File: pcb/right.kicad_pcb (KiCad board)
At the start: 2 copper layers, 135 x 95.7 mm, 50 parts, among them SW1 SW_PUSH, SW10 SW_PUSH, SW11 SW_PUSH, SW12 SW_PUSH, SW13 SW_PUSH, SW14 SW_PUSH, SW15 SW_PUSH, SW16 SW_PUSH, SW17 SW_PUSH, SW18 SW_PUSH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

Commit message: update cases, extra hole on right side
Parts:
- added H8: MountingHole, kbd:M2_HOLE_v2, F.Cu at (91.0, 61.0)
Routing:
- net col3: track 137.9 -> 136.3 mm
- net ENCB: track 63.0 -> 64.1 mm
- net col4: track 113.5 -> 113.0 mm

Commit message: improve rotary encoder footprint
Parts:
- RE1: footprint pica:RotaryEncoder_EC11-no-legs -> pica:RotaryEncoder_EC11
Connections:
- RE1 pad S1: unconnected-(RE1-PadS1) -> (no net)
- RE1 pad S2: unconnected-(RE1-PadS2) -> (no net)
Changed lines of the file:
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@@
   (net 32 "row6")
   (net 33 "row7")
-  (net 34 "unconnected-(RE1-PadS2)")
-  (net 35 "unconnected-(RE1-PadS1)")
   (footprint "pica:CherryMX_Hotswap" (layer "F.Cu")
     (at 153 99)
@@
     )
   )
-  (footprint "pica:RotaryEncoder_EC11-no-legs" (layer "F.Cu")
+  (footprint "pica:RotaryEncoder_EC11" (layer "F.Cu")
     (at 95.5 74 -90)
     (descr "Alps rotary encoder, EC12E... with switch, vertical shaft, http://www.alps.com/prod/info/E/HTML/Encoder/Incremental/EC11/EC11E15204A3.html")
@@
     (property "Sheetname" "")
     (attr through_hole)
-    (fp_text reference "RE1" (at -4.7 -7.2 90) (layer "F.Fab")
+    (fp_text reference "RE1" (at -4.7 -7.2 -90) (layer "F.Fab")
       (effects (font (size 1 1) (thickness 0.15)))
     )
-    (fp_text value "RotaryEncoder_Switch" (at 0 7.9 90) (layer "F.Fab")
-      (effects (font (size 1 1) (thickness 0.15)))
-    )
-    (fp_text user "${REFERENCE}" (at 3.6 3.8 90) (layer "F.Fab")
+    (fp_text value "RotaryEncoder_Switch" (at 0 7.9 -90) (layer "F.Fab")
       (effects (font (size 1 1) (thickness 0.15)))
     )
+    (fp_line (start -0.5 0) (end 0.5 0) (layer "F.SilkS") (width 0.12))
+    (fp_line (start 6.1 5.9) (end 2 5.9) (layer "F.SilkS") (width 0.12))
     (fp_line (start -2 5.9) (end -6.1 5.9) (layer "F.SilkS") (width 0.12))
+    (fp_line (start 6.1 3.5) (end 6.1 5.9) (layer "F.SilkS") (width 0.12))
     (fp_line (start 6.1 -5.9) (end 6.1 -3.5) (layer "F.SilkS") (width 0.12))
-    (fp_line (start 6.1 5.9) (end 2 5.9) (layer "F.SilkS") (width 0.12))
+    (fp_line (start -6.1 -5.9) (end -6.1 5.9) (layer "F.SilkS") (width 0.12))
     (fp_line (start -2 -5.9) (end -6.1 -5.9) (layer "F.SilkS") (width 0.12))
     (fp_line (start 0 -0.5) (end 0 0.5) (layer "F.SilkS") (width 0.12))
-    (fp_line (start -6.1 -5.9) (end -6.1 5.9) (layer "F.SilkS") (width 0.12))
     (fp_line (start 6.1 -1.3) (end 6.1 1.3) (layer "F.SilkS") (width 0.12))
-    (fp_line (start -0.5 0) (end 0.5 0) (layer "F.SilkS") (width 0.12))
     (fp_line (start 2 -5.9) (end 6.1 -5.9) (layer "F.SilkS") (width 0.12))
-    (fp_line (start 6.1 3.5) (end 6.1 5.9) (layer "F.SilkS") (width 0.12))
     (fp_circle (center 0 0) (end 3 0) (layer "F.SilkS") (width 0.12) (fill none))
-    (fp_line (start 8.5 7.1) (end 8.5 -7.1) (layer "F.CrtYd") (width 0.05))
     (fp_line (start -9 -7.1) (end 8.5 -7.1) (layer "F.CrtYd") (width 0.05))
     (fp_line (start -9 -7.1) (end -9 7.1) (layer "F.CrtYd") (width 0.05))
     (fp_line (start 8.5 7.1) (end -9 7.1) (layer "F.CrtYd") (width 0.05))
-    (fp_line (start 6 5.8) (end -6 5.8) (layer "F.Fab") (width 0.12))
-    (fp_line (start 6 -5.8) (end 6 5.8) (layer "F.Fab") (width 0.12))
-    (fp_line (start -6 5.8) (end -6 -4.7) (layer "F.Fab") (width 0.12))
+    (fp_line (start 8.5 7.1) (end 8.5 -7.1) (layer "F.CrtYd") (width 0.05))
     (fp_line (start -6 -4.7) (end -5 -5.8) (layer "F.Fab") (width 0.12))
+    (fp_line (start 0 -3) (end 0 3) (layer "F.Fab") (width 0.12))
+    (fp_line (start -6 5.8) (end -6 -4.7) (layer "F.Fab") (width 0.12))
+    (fp_line (start 6 -5.8) (end 6 5.8) (layer "F.Fab") (width 0.12))
+    (fp_line (start -3 0) (end 3 0) (layer "F.Fab") (width 0.12))
     (fp_line (start -5 -5.8) (end 6 -5.8) (layer "F.Fab") (width 0.12))
+    (fp_line (start 6 5.8) (end -6 5.8) (layer "F.Fab") (width 0.12))
+    (fp_circle (center 0 0) (end 3 0) (layer "F.Fab") (width 0.12) (fill none))
+    (pad "" np_thru_hole oval (at 0 5.6 270) (size 3.2 2) (drill oval 2.8 1.5) (layers F&B.Cu "B.Mask"))
+    (pad "" np_thru_hole oval (at 0 -5.6 270) (size 3.2 2) (drill oval 2.8 1.5) (layers F&B.Cu "B.Mask"))
     (pad "A" thru_hole circle (at -7.5 -2.5 270) (size 2 2) (drill 1) (layers *.Cu "B.SilkS" "B.Mask")
       (net 24 "ENCA") (pinfunction "A") (pintype "passive"))
@@
       (net 2 "GND") (pinfunction "C") (pintype "passive"))
     (pad "S1" thru_hole circle (at 7 2.5 270) (size 2 2) (drill 1) (layers *.Cu "B.Mask")
-      (net 35 "unconnected-(RE1-PadS1)") (pinfunction "S1") (pintype "passive+no_connect"))
+      (pinfunction "S1") (pintype "passive+no_connect"))
     (pad "S2" thru_hole circle (at 7 -2.5 270) (size 2 2) (drill 1) (layers *.Cu "B.Mask")
-      (net 34 "unconnected-(RE1-PadS2)") (pinfunction "S2") (pintype "passive+no_connect"))
+      (pinfunction "S2") (pintype "passive+no_connect"))
     (model "../footprints/Rotary Encoder.step"
       (offset (xyz -6 6 0))

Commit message: v2
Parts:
- removed H8: MountingHole, kbd:M2_HOLE_v2
- added BATTCONN1: Conn_01x02_Female, pica:JST_PH_S2B-PH-K_1x02_P2.00mm, F.Cu at (88.0, 81.3)
- added BATTCONN2: Conn_01x02_Female, pica:JST_PH_S2B-PH-K_1x02_P2.00mm, F.Cu at (145.0, 102.8)
- added BATTSW1: SW_SPDT, Button_Switch_SMD:SW_SPDT_PCM12, F.Cu at (84.0, 76.8)
- added JP1: SolderJumper_2_Open, Jumper:SolderJumper-2_P1.3mm_Open_TrianglePad1.0x1.5mm, B.Cu at (97.7, 81.6)
- added JP2: SolderJumper_2_Open, Jumper:SolderJumper-2_P1.3mm_Open_TrianglePad1.0x1.5mm, F.Cu at (97.7, 81.6)
- added RE2: RotaryEncoder_Switch, pica:RotaryEncoder_EC11, F.Cu at (160.2, 113.6)
- added U1: xiao-ble, pica:xiao-ble-tht, F.Cu at (92.0, 61.9)
- G***: moved to B.Cu
- H1, H2, H3, H4, H5: footprint kbd:M2_HOLE_v2 -> pica:spacer_m2_3.4
- H6, H7: footprint kbd:M2_Hole_TH -> kbd:thread_m2
- SW1, SW10, SW11, SW12, SW13, SW14, SW15, SW16, SW17, SW18, SW19, SW2, SW3, SW4, SW5, SW6, SW7, SW8, SW9: footprint pica:CherryMX_Hotswap -> pica:CherryMX_Hotswap_ChocV2
- SW20: footprint pica:CherryMX_Hotswap_1.5 -> pica:CherryMX_Hotswap_ChocV2_1.5
- USB1: footprint typec:HRO-TYPE-C-31-M-12-HandSoldering -> pica:HRO-TYPE-C-31-M-12-data
- moved H6 32.1 mm to (97.5, 74.8)
- moved H7 31.9 mm to (88.7, 74.8)
- moved RE1 20.5 mm to (91.5, 94.1), turned to 180 degrees
- moved D18 10.0 mm to (140.4, 104.8)
- moved D12 9.81 mm to (168.4, 101.8)
- moved D13 9.81 mm to (149.4, 97.8)
- moved D7 9.81 mm to (168.4, 82.8)
- moved D8 9.81 mm to (149.4, 78.8)
- moved H4 9.81 mm to (157.9, 99.8)
- moved SW12 9.81 mm to (168.4, 93.8)
- moved SW13 9.81 mm to (149.4, 89.8)
- moved SW18 9.81 mm to (140.4, 113.3)
- moved SW7 9.81 mm to (168.4, 74.8)
- moved SW8 9.81 mm to (149.4, 70.8)
- moved D10 9.81 mm to (111.5, 85.3)
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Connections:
- D1 pad 1: row7 -> row0_r
- D10 pad 1: row6 -> row1_r
- D11 pad 1: row5 -> row2_r
- D12 pad 1: row5 -> row2_r
- D13 pad 1: row5 -> row2_r
- D14 pad 1: row5 -> row2_r
- D15 pad 1: row5 -> row2_r
- D16 pad 1: row4 -> row3_r
- D17 pad 1: row4 -> row3_r
- D18 pad 1: row4 -> row3_r
- D19 pad 1: row4 -> row3_r
- D2 pad 1: row7 -> row0_r
- D20 pad 1: row4 -> row3_r
- D3 pad 1: row7 -> row0_r
- D4 pad 1: row7 -> row0_r
- D5 pad 1: row7 -> row0_r
- D6 pad 1: row6 -> row1_r
- D7 pad 1: row6 -> row1_r
- D8 pad 1: row6 -> row1_r
- D9 pad 1: row6 -> row1_r
- RE1 pad A: ENCA -> ENCA_r
- RE1 pad B: ENCB -> ENCB_r
- RE1 pad C: GND -> GNDA
- RE1 pad S1: (no net) -> unconnected-(RE1-PadS1)
- RE1 pad S2: (no net) -> unconnected-(RE1-PadS2)
- SW1 pad 2: col0 -> col0_r
- SW10 pad 2: col4 -> col4_r
- SW11 pad 2: col0 -> col0_r
- SW12 pad 2: col1 -> col1_r
- SW13 pad 2: col2 -> col2_r
- SW14 pad 2: col3 -> col3_r
- SW15 pad 2: col4 -> col4_r
- SW16 pad 2: col0 -> col0_r
- SW17 pad 2: col1 -> col1_r
- SW18 pad 2: col2 -> col2_r
- SW19 pad 2: col3 -> col3_r
- SW2 pad 2: col1 -> col1_r
- SW20 pad 2: col4 -> col4_r
- SW3 pad 2: col2 -> col2_r
- SW4 pad 2: col3 -> col3_r
- SW5 pad 2: col4 -> col4_r
- SW6 pad 2: col0 -> col0_r
- SW7 pad 2: col1 -> col1_r
- SW8 pad 2: col2 -> col2_r
- SW9 pad 2: col3 -> col3_r
- USB1 pad 1: GND -> GNDA
- USB1 pad 11: ENCA -> VDD
- USB1 pad 12: ENCB -> GNDA
- USB1 pad 2: row7 -> VDD
- USB1 pad 5: row4 -> ENCB_r
- USB1 pad 6: col4 -> DATA_r
- USB1 pad 7: col3 -> ENCB_r
- USB1 pad 8: col2 -> DATA_r
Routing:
- net col0: track 249.3 -> 0.00 mm, vias 4 -> 0
- net col0_r: track 0.00 -> 238.8 mm
- net col1_r: track 0.00 -> 234.7 mm
- net col1: track 226.0 -> 0.00 mm, vias 4 -> 0
- net col2_r: track 0.00 -> 185.2 mm
- net row3_r: track 0.00 -> 183.7 mm
- net col3_r: track 0.00 -> 166.0 mm
- net col2: track 158.9 -> 0.00 mm, vias 4 -> 0
- net col4_r: track 0.00 -> 153.7 mm
- net row4: track 152.3 -> 0.00 mm, vias 1 -> 0
- net row7: track 143.8 -> 0.00 mm, vias 1 -> 0
- net col3: track 136.3 -> 0.00 mm, vias 4 -> 0
- net ENCB_r: track 0.00 -> 134.6 mm, vias 0 -> 1
- net row2_r: track 0.00 -> 133.2 mm
- net row5: track 132.9 -> 0.00 mm, vias 1 -> 0
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- added copper zone on B.Cu, net GNDA
- added copper zone on F.Cu, net GNDA
- removed copper zone on B.Cu, net GND
- removed copper zone on F.Cu, net GND
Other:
- board size 135 x 95.7 mm -> 137.8 x 95.7 mm
- board text added: "B+"
- board text added: "OFF"
- board text added: "Pica40 v2"
- board text added: "wired"
- board text added: "wireless"
- board text removed: "JLCJLCJLCJLC"
- board text removed: "PicaPica"

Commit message: remove second encoder
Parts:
- removed RE2: RotaryEncoder_Switch, pica:RotaryEncoder_EC11
- added G***: LOGO, pica:logo, F.Cu at (162.8, 111.1)
- moved G*** 1.28 mm to (162.8, 111.1)
- moved SW11 0.11 mm to (187.4, 105.5)
- moved SW16 0.11 mm to (208.5, 82.8)
- moved SW17 0.11 mm to (206.8, 101.8)
- moved SW6 0.11 mm to (189.1, 86.6)
- moved D20 0.11 mm to (97.3, 106.5)
- moved D2 0.11 mm to (168.5, 63.8)
- moved D3 0.11 mm to (149.5, 59.8)
- moved SW2 0.11 mm to (168.5, 55.8)
- moved SW3 0.11 mm to (149.5, 51.8)
- moved SW4 0.11 mm to (130.5, 56.2)
- moved BATTCONN2 0.11 mm to (145.1, 102.8)
- moved D1 0.11 mm to (190.0, 75.7)
- moved D11 0.11 mm to (188.1, 97.1)
- moved D12 0.11 mm to (168.5, 101.8)
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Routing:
- net ENCA_r: track 97.8 -> 16.1 mm
- net ENCB_r: track 134.6 -> 62.3 mm, vias 1 -> 0
- net col1_r: track 234.7 -> 231.6 mm
- net row3_r: track 183.7 -> 184.8 mm
- net GNDA: vias 2 -> 3
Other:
- outline, holes or cut-outs redrawn

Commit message: udpate pcb, remove unused files
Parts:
- removed BATTCONN1, BATTCONN2: Conn_01x02_Female, pica:JST_PH_S2B-PH-K_1x02_P2.00mm
- removed BATTSW1: SW_SPDT, Button_Switch_SMD:SW_SPDT_PCM12
- removed D1, D10, D11, D12, D13, D14, D15, D16, D17, D18, D19, D2, D20, D3, D4, D5, D6, D7, D8, D9: D_Small, pica:D3_SMD
- removed H1, H2, H3, H4, H5: MountingHole, pica:spacer_m2_3.4
- removed H6, H7: MountingHole, kbd:thread_m2
- removed JP1, JP2: SolderJumper_2_Open, Jumper:SolderJumper-2_P1.3mm_Open_TrianglePad1.0x1.5mm
- removed RE1: RotaryEncoder_Switch, pica:RotaryEncoder_EC11
- removed SW1, SW10, SW11, SW12, SW13, SW14, SW15, SW16, SW17, SW18, SW19, SW2, SW3, SW4, SW5, SW6, SW7, SW8, SW9: SW_PUSH, pica:CherryMX_Hotswap_ChocV2
- removed SW20: SW_PUSH, pica:CherryMX_Hotswap_ChocV2_1.5
- removed U1: xiao-ble, pica:xiao-ble-tht
- removed USB1: HRO-TYPE-C-31-M-12, pica:HRO-TYPE-C-31-M-12-data
- added BATTCONN3: Conn_01x02_Female, pica:JST_PH_S2B-PH-K_1x02_P2.00mm, F.Cu at (90.8, 81.8)
- added BATTCONN4: Conn_01x02_Female, pica:JST_PH_S2B-PH-K_1x02_P2.00mm, F.Cu at (150.8, 99.5)
- added BATTSW2: SW_SPDT, Button_Switch_SMD:SW_SPDT_PCM12, B.Cu at (89.8, 72.0)
- added D21: D_Small, pica:D3_SMD, B.Cu at (195.7, 72.5)
- added D22: D_Small, pica:D3_SMD, B.Cu at (174.2, 60.5)
- added D23: D_Small, pica:D3_SMD, B.Cu at (155.2, 56.5)
- added D24: D_Small, pica:D3_SMD, B.Cu at (136.2, 61.0)
- added D25: D_Small, pica:D3_SMD, B.Cu at (117.2, 63.0)
- added D26: D_Small, pica:D3_SMD, B.Cu at (194.1, 91.2)
- added D27: D_Small, pica:D3_SMD, B.Cu at (174.2, 79.5)
- added D28: D_Small, pica:D3_SMD, B.Cu at (155.2, 75.5)
- added D29: D_Small, pica:D3_SMD, B.Cu at (136.2, 80.0)
- added D30: D_Small, pica:D3_SMD, B.Cu at (117.2, 82.0)
- added D31: D_Small, pica:D3_SMD, B.Cu at (193.8, 93.9)
- added D32: D_Small, pica:D3_SMD, B.Cu at (174.2, 98.5)
- added D33: D_Small, pica:D3_SMD, B.Cu at (155.2, 94.5)
- added D34: D_Small, pica:D3_SMD, B.Cu at (136.2, 99.0)
- added D35: D_Small, pica:D3_SMD, B.Cu at (117.2, 101.0)
- added D36: D_Small, pica:D3_SMD, B.Cu at (213.6, 87.5)
- added D37: D_Small, pica:D3_SMD, B.Cu at (213.4, 89.9)
- added D38: D_Small, pica:D3_SMD, B.Cu at (146.2, 101.5)
- added D39: D_Small, pica:D3_SMD, B.Cu at (127.2, 102.5)
- added D40: D_Small, pica:D3_SMD, B.Cu at (103.0, 103.3)
- added G***: LOGO, pica:seeed-logo, F.Cu at (98.8, 74.0)
- added H10: MountingHole, pica:spacer_m2_3.4, B.Cu at (204.5, 88.2)
- added H11: MountingHole, pica:spacer_m2_3.4, B.Cu at (163.8, 96.5)
- added H12: MountingHole, pica:spacer_m2_3.4, B.Cu at (125.8, 64.5)
- added H13: MountingHole, kbd:thread_m2, B.Cu at (103.2, 71.5)
- added H14: MountingHole, kbd:thread_m2, B.Cu at (94.5, 71.5)
- added H8: MountingHole, pica:spacer_m2_3.4, B.Cu at (184.9, 62.0)
- added H9: MountingHole, pica:spacer_m2_3.4, B.Cu at (112.2, 110.5)
- added J2: MJ-4PP-9, pica:MJ-4PP-9_1side, F.Cu at (87.5, 79.8)
- added JP4: SolderJumper_2_Open, Jumper:SolderJumper-2_P1.3mm_Open_TrianglePad1.0x1.5mm, F.Cu at (101.8, 78.2)
- added JP5: SolderJumper_2_Open, Jumper:SolderJumper-2_P1.3mm_Open_TrianglePad1.0x1.5mm, B.Cu at (104.2, 78.2)
- added JP6: SolderJumper_2_Open, Jumper:SolderJumper-2_P1.3mm_Open_TrianglePad1.0x1.5mm, F.Cu at (104.2, 78.2)
- added RE2: RotaryEncoder_Switch, pica:RotaryEncoder_EC11, F.Cu at (97.2, 90.8)
- added SW21: SW_PUSH, pica:CherryMX_Hotswap_ChocV2, F.Cu at (196.4, 64.4)
- added SW22: SW_PUSH, pica:CherryMX_Hotswap_ChocV2, F.Cu at (174.2, 52.5)
- added SW23: SW_PUSH, pica:CherryMX_Hotswap_ChocV2, F.Cu at (155.2, 48.5)
- added SW24: SW_PUSH, pica:CherryMX_Hotswap_ChocV2, F.Cu at (136.2, 53.0)
- added SW25: SW_PUSH, pica:CherryMX_Hotswap_ChocV2, F.Cu at (117.2, 55.0)
- added SW26: SW_PUSH, pica:CherryMX_Hotswap_ChocV2, F.Cu at (194.8, 83.3)
- added SW27: SW_PUSH, pica:CherryMX_Hotswap_ChocV2, F.Cu at (174.2, 71.5)
- added SW28: SW_PUSH, pica:CherryMX_Hotswap_ChocV2, F.Cu at (155.2, 67.5)
- added SW29: SW_PUSH, pica:CherryMX_Hotswap_ChocV2, F.Cu at (136.2, 72.0)
- added SW30: SW_PUSH, pica:CherryMX_Hotswap_ChocV2, F.Cu at (117.2, 74.0)
- added SW31: SW_PUSH, pica:CherryMX_Hotswap_ChocV2, F.Cu at (193.2, 102.3)
- added SW32: SW_PUSH, pica:CherryMX_Hotswap_ChocV2, F.Cu at (174.2, 90.5)
- added SW33: SW_PUSH, pica:CherryMX_Hotswap_ChocV2, F.Cu at (155.2, 86.5)
- added SW34: SW_PUSH, pica:CherryMX_Hotswap_ChocV2, F.Cu at (136.2, 91.0)
- added SW35: SW_PUSH, pica:CherryMX_Hotswap_ChocV2, F.Cu at (117.2, 93.0)
- added SW36: SW_PUSH, pica:CherryMX_Hotswap_ChocV2, F.Cu at (214.2, 79.6)
- added SW37: SW_PUSH, pica:CherryMX_Hotswap_ChocV2, F.Cu at (212.6, 98.6)
- added SW38: SW_PUSH, pica:CherryMX_Hotswap_ChocV2, F.Cu at (146.2, 110.0)
- added SW39: SW_PUSH, pica:CherryMX_Hotswap_ChocV2, F.Cu at (125.0, 112.8)
- added SW40: SW_PUSH, pica:CherryMX_Hotswap_ChocV2_1.5, F.Cu at (102.8, 116.5)
- added U2: xiao-ble, pica:xiao-ble-tht, F.Cu at (97.8, 58.5)
- added USB2: HRO-TYPE-C-31-M-12, pica:HRO-TYPE-C-31-M-12-data, F.Cu at (87.2, 103.8)
- moved G*** 6.60 mm to (168.5, 107.8) (x2)
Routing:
- net VDD: track 61.6 -> 91.6 mm
- net ENCA_r: track 16.1 -> 42.7 mm, vias 0 -> 1
- net Net-(D39-Pad2): track 0.00 -> 21.3 mm
- net Net-(D19-Pad2): track 21.3 -> 0.00 mm
- net Net-(JP5-Pad2): track 0.00 -> 19.5 mm, vias 0 -> 1
- net Net-(JP1-Pad2): track 18.7 -> 0.00 mm, vias 1 -> 0
- net Net-(D38-Pad2): track 0.00 -> 16.1 mm
- net Net-(D18-Pad2): track 16.1 -> 0.00 mm
- net Net-(D37-Pad2): track 0.00 -> 16.1 mm
- net Net-(D17-Pad2): track 16.1 -> 0.00 mm
- net Net-(D31-Pad2): track 0.00 -> 15.9 mm
- net Net-(D11-Pad2): track 15.9 -> 0.00 mm
- net Net-(D40-Pad2): track 0.00 -> 13.1 mm
- net Net-(D20-Pad2): track 13.1 -> 0.00 mm
- net Net-(D6-Pad2): track 12.9 -> 0.00 mm
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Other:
- outline, holes or cut-outs redrawn
- board text added: "JLCJLCJLCJLC"
- board text added: "no enc"

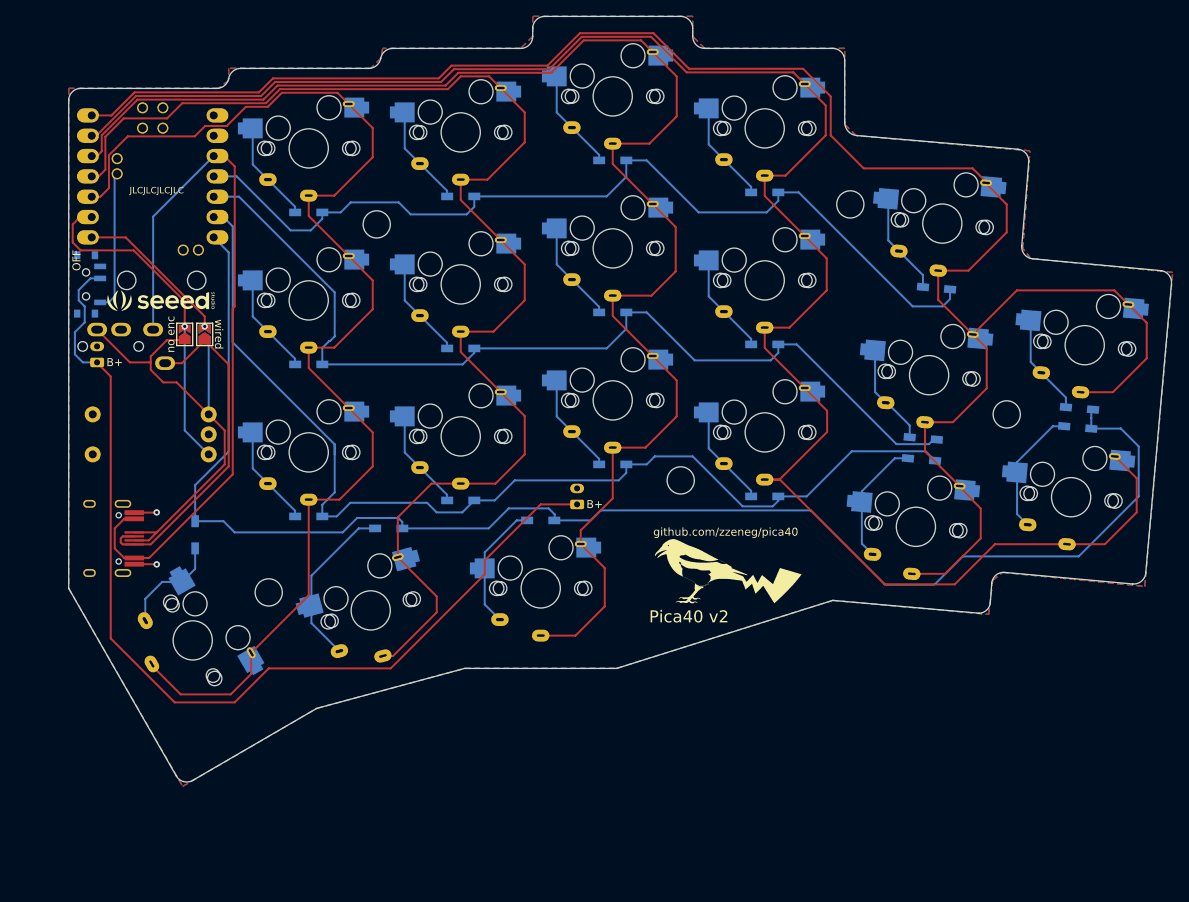
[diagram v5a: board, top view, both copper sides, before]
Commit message: improve footprints and routing
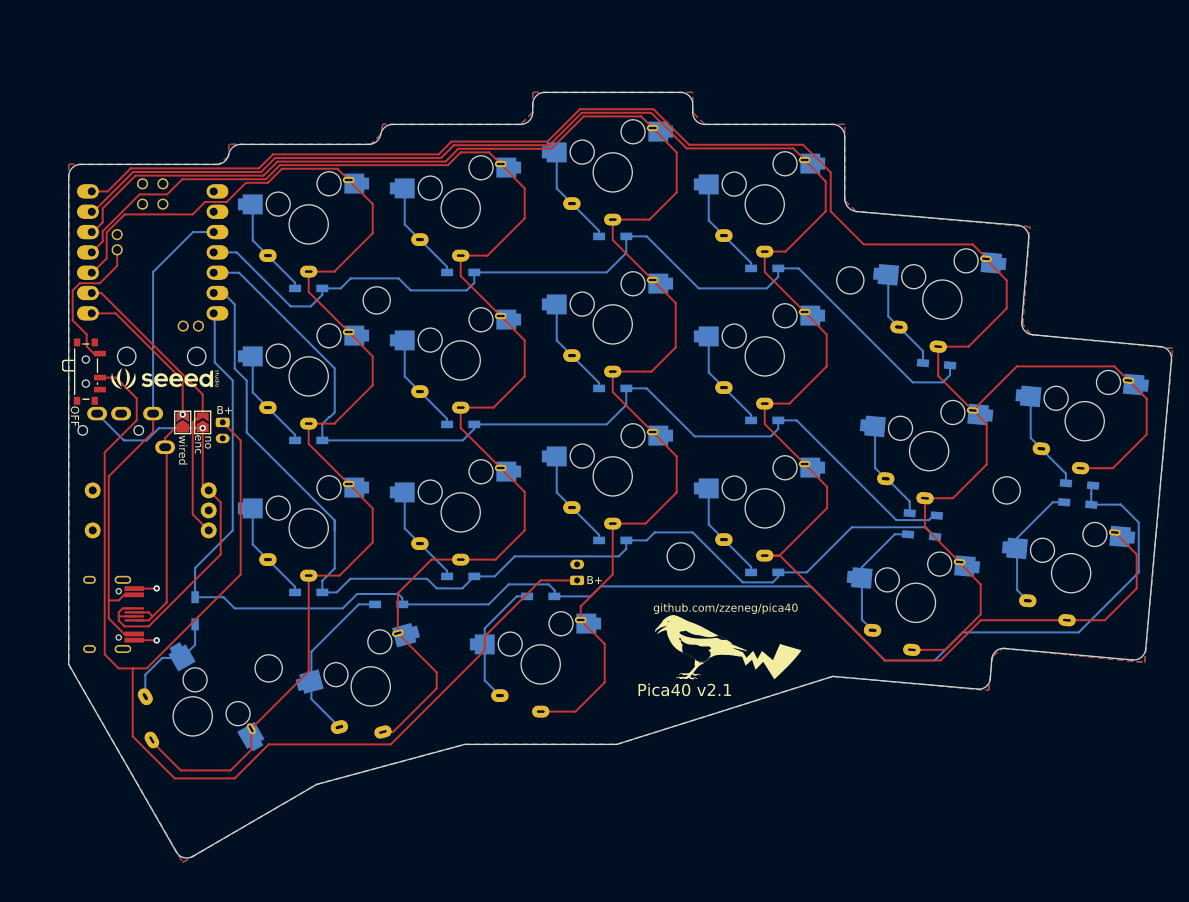
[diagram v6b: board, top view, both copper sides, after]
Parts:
- BATTSW2: moved to F.Cu
- moved BATTCONN3 17.4 mm to (106.5, 89.2), turned to -90 degrees
- moved JP5 11.3 mm to (101.5, 89.2)
- moved JP6 11.3 mm to (101.5, 89.2)
- moved JP4 11.2 mm to (104.0, 89.2)
- moved BATTSW2 10.9 mm to (89.7, 82.9), turned to -90 degrees
- moved J2 10.5 mm to (87.5, 90.2)
- moved G*** 9.76 mm to (99.2, 83.8)
- moved BATTCONN4 9.50 mm to (150.8, 109.0)
- moved D21 9.50 mm to (195.7, 82.0)
- moved D22 9.50 mm to (174.2, 70.0)
- moved D23 9.50 mm to (155.2, 66.0)
- moved D24 9.50 mm to (136.2, 70.5)
- moved D25 9.50 mm to (117.2, 72.5)
- moved D26 9.50 mm to (194.1, 100.8)
- moved D27 9.50 mm to (174.2, 89.0)
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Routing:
- net BATT_r: track 123.4 -> 159.4 mm
- net VDD: track 91.6 -> 62.7 mm
- net DATA_r: track 43.1 -> 30.8 mm
- net ENCB_r: track 59.3 -> 53.8 mm, vias 0 -> 1
- net ENCA_r: track 42.7 -> 37.8 mm, vias 1 -> 0
- net col3_r: track 166.0 -> 164.3 mm
- net RAW_r: track 17.6 -> 18.6 mm
- net col4_r: track 153.7 -> 153.2 mm
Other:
- board text added: "Pica40 v2.1"
- board text added: "enc"
- board text added: "no"
- board text removed: "JLCJLCJLCJLC"
- board text removed: "Pica40 v2"
- board text removed: "no enc"
